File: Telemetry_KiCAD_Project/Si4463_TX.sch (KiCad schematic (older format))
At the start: 14 parts, among them U2 Si4463, Y1 30MHz

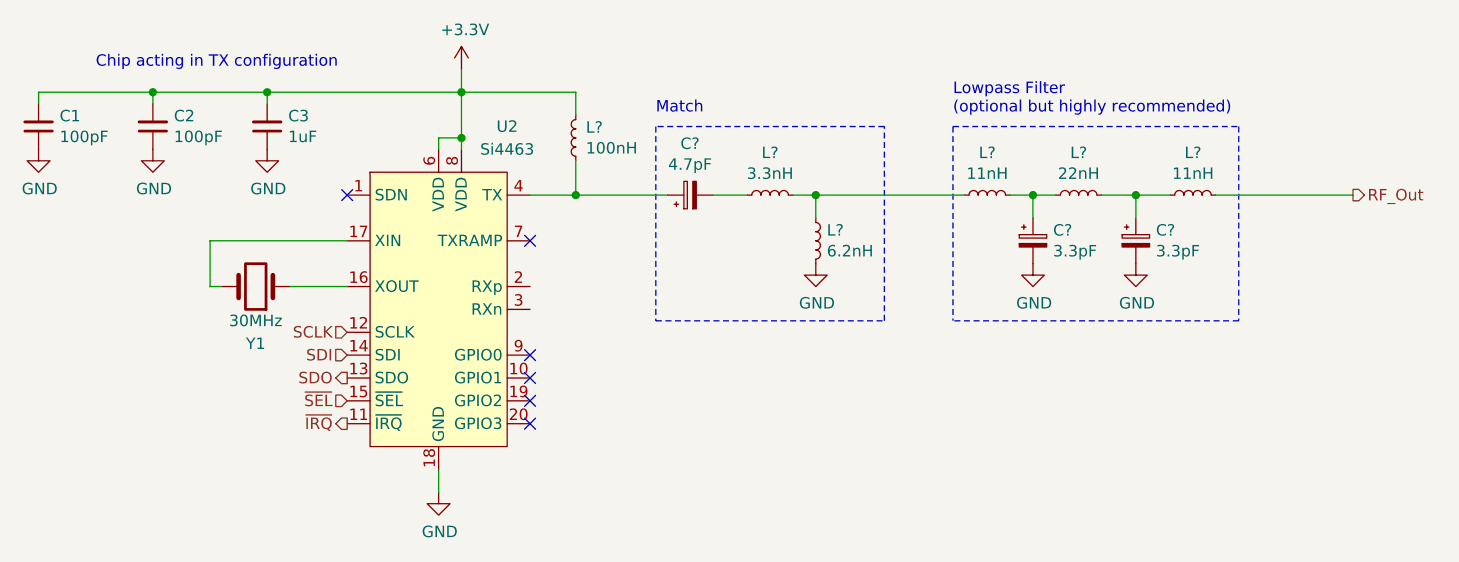
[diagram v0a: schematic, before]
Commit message: Added TX/RX matching network passives to PCB
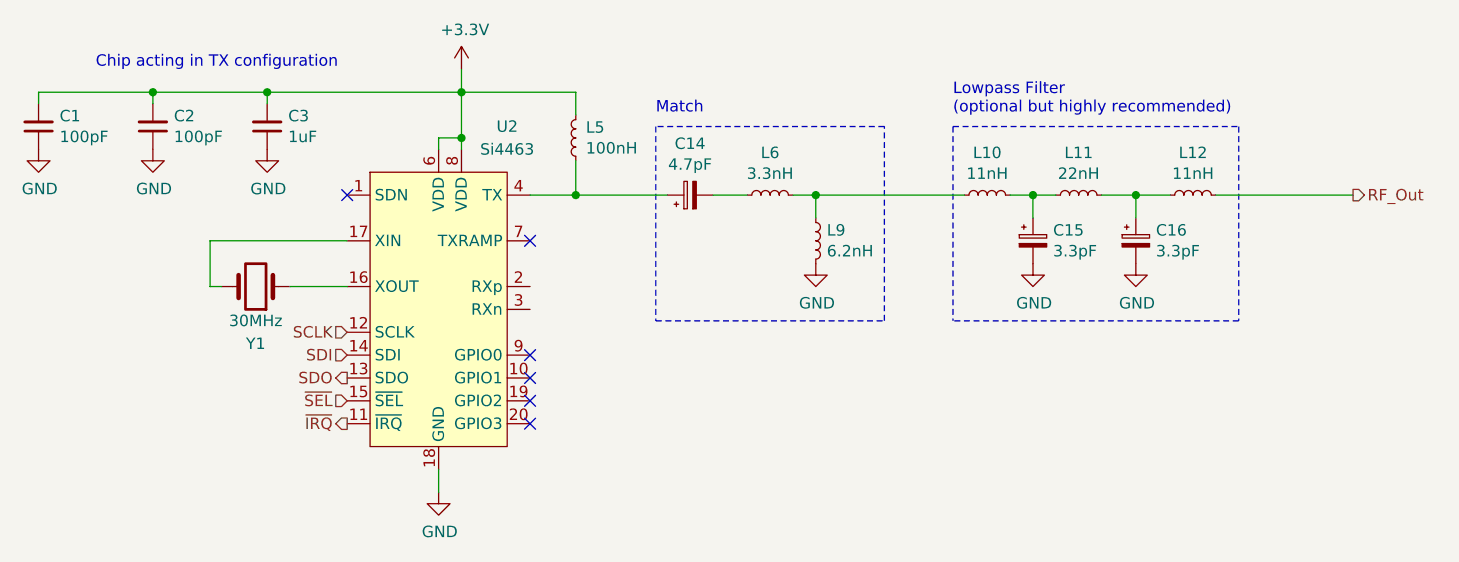
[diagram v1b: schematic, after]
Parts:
- C14, C15, C16: renamed from C?; footprint (none) -> Capacitor_SMD:C_0603_1608Metric
- L10, L11, L12, L5, L6, L9: renamed from L?; footprint (none) -> Inductor_SMD:L_0603_1608Metric
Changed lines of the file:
@@
 $Comp
 L power:GND #PWR0104
-U 1 1 619DAEC1
+U 1 1 61AFA3CA
 P 6150 4450
-AR Path="/619D9C89/619DAEC1" Ref="#PWR0104"  Part="1"
-AR Path="/61A0416A/619DAEC1" Ref="#PWR0116"  Part="1"
+AR Path="/619D9C89/61AFA3CA" Ref="#PWR0104"  Part="1"
+AR Path="/61A0416A/61AFA3CA" Ref="#PWR0116"  Part="1"
 F 0 "#PWR0104" H 6150 4200 50  0001 C CNN
 F 1 "GND" H 6155 4277 50  0000 C CNN
@@
 $Comp
 L Device:C_Small C3
-U 1 1 619F7D57
+U 1 1 61AFA3CC
 P 5400 2850
-AR Path="/619D9C89/619F7D57" Ref="C3"  Part="1"
-AR Path="/61A0416A/619F7D57" Ref="C13"  Part="1"
+AR Path="/619D9C89/61AFA3CC" Ref="C3"  Part="1"
+AR Path="/61A0416A/61AFA3CC" Ref="C13"  Part="1"
 F 0 "C3" H 5308 2804 50  0000 R CNN
 F 1 "1uF" H 5308 2895 50  0000 R CNN
@@
 $Comp
 L Device:C_Small C2
-U 1 1 619F860E
+U 1 1 61AFA3CD
 P 4900 2850
-AR Path="/619D9C89/619F860E" Ref="C2"  Part="1"
-AR Path="/61A0416A/619F860E" Ref="C12"  Part="1"
+AR Path="/619D9C89/61AFA3CD" Ref="C2"  Part="1"
+AR Path="/61A0416A/61AFA3CD" Ref="C12"  Part="1"
 F 0 "C2" H 4808 2804 50  0000 R CNN
 F 1 "100pF" H 4808 2895 50  0000 R CNN
@@
 $Comp
 L Device:C_Small C1
-U 1 1 619F8BD8
+U 1 1 61AFA3CE
 P 4400 2850
-AR Path="/619D9C89/619F8BD8" Ref="C1"  Part="1"
-AR Path="/61A0416A/619F8BD8" Ref="C11"  Part="1"
+AR Path="/619D9C89/61AFA3CE" Ref="C1"  Part="1"
+AR Path="/61A0416A/61AFA3CE" Ref="C11"  Part="1"
 F 0 "C1" H 4308 2804 50  0000 R CNN
 F 1 "100pF" H 4308 2895 50  0000 R CNN
@@
 $Comp
 L power:GND #PWR0109
-U 1 1 619F9745
+U 1 1 61AFA3CF
 P 4400 2950
-AR Path="/619D9C89/619F9745" Ref="#PWR0109"  Part="1"
-AR Path="/61A0416A/619F9745" Ref="#PWR0121"  Part="1"
+AR Path="/619D9C89/61AFA3CF" Ref="#PWR0109"  Part="1"
+AR Path="/61A0416A/61AFA3CF" Ref="#PWR0121"  Part="1"
 F 0 "#PWR0109" H 4400 2700 50  0001 C CNN
 F 1 "GND" H 4405 2777 50  0000 C CNN
@@
 $Comp
 L power:GND #PWR0111
-U 1 1 619F9CE2
+U 1 1 61AFA3D1
 P 5400 2950
-AR Path="/619D9C89/619F9CE2" Ref="#PWR0111"  Part="1"
-AR Path="/61A0416A/619F9CE2" Ref="#PWR0123"  Part="1"
+AR Path="/619D9C89/61AFA3D1" Ref="#PWR0111"  Part="1"
+AR Path="/61A0416A/61AFA3D1" Ref="#PWR0123"  Part="1"
 F 0 "#PWR0111" H 5400 2700 50  0001 C CNN
 F 1 "GND" H 5405 2777 50  0000 C CNN
@@
 NoConn ~ 5750 3150
 $Comp
-L Device:L_Small L?
+L Device:L_Small L5
 U 1 1 61AC1A40
 P 6750 2900
-AR Path="/619D9C89/61AC1A40" Ref="L?"  Part="1"
+AR Path="/619D9C89/61AC1A40" Ref="L5"  Part="1"
 AR Path="/61A0416A/61AC1A40" Ref="L?"  Part="1"
-F 0 "L?" H 6706 2854 50  0000 R CNN
+F 0 "L5" H 6706 2854 50  0000 R CNN
 F 1 "100nH" H 6706 2945 50  0000 R CNN
-F 2 "" H 6750 2900 50  0001 C CNN
+F 2 "Inductor_SMD:L_0603_1608Metric" H 6750 2900 50  0001 C CNN
 F 3 "~" H 6750 2900 50  0001 C CNN
 	1    6750 2900
@@
 Connection ~ 6750 3150
 $Comp
-L Device:L_Small L?
+L Device:L_Small L6
 U 1 1 61AC64F7
 P 7600 3150
-AR Path="/619D9C89/61AC64F7" Ref="L?"  Part="1"
+AR Path="/619D9C89/61AC64F7" Ref="L6"  Part="1"
 AR Path="/61A0416A/61AC64F7" Ref="L?"  Part="1"
-F 0 "L?" V 7785 3150 50  0000 C CNN
+F 0 "L6" V 7785 3150 50  0000 C CNN
 F 1 "3.3nH" V 7694 3150 50  0000 C CNN
-F 2 "" H 7600 3150 50  0001 C CNN
+F 2 "Inductor_SMD:L_0603_1608Metric" H 7600 3150 50  0001 C CNN
 F 3 "~" H 7600 3150 50  0001 C CNN
 	1    7600 3150
@@
 	7350 3150 7500 3150
 $Comp
-L Device:L_Small L?
+L Device:L_Small L9
 U 1 1 61AC7786
 P 7800 3350
-AR Path="/619D9C89/61AC7786" Ref="L?"  Part="1"
+AR Path="/619D9C89/61AC7786" Ref="L9"  Part="1"
 AR Path="/61A0416A/61AC7786" Ref="L?"  Part="1"
-F 0 "L?" H 7848 3396 50  0000 L CNN
+F 0 "L9" H 7848 3396 50  0000 L CNN
 F 1 "6.2nH" H 7848 3305 50  0000 L CNN
-F 2 "" H 7800 3350 50  0001 C CNN
+F 2 "Inductor_SMD:L_0603_1608Metric" H 7800 3350 50  0001 C CNN
 F 3 "~" H 7800 3350 50  0001 C CNN
 	1    7800 3350
@@
 	7800 3250 7800 3150
 $Comp
-L power:GND #PWR?
+L power:GND #PWR011
 U 1 1 61AC819F
 P 7800 3450
-AR Path="/619D9C89/61AC819F" Ref="#PWR?"  Part="1"
+AR Path="/619D9C89/61AC819F" Ref="#PWR011"  Part="1"
 AR Path="/61A0416A/61AC819F" Ref="#PWR?"  Part="1"
-F 0 "#PWR?" H 7800 3200 50  0001 C CNN
+F 0 "#PWR011" H 7800 3200 50  0001 C CNN
 F 1 "GND" H 7805 3277 50  0000 C CNN
 F 2 "" H 7800 3450 50  0001 C CNN
@@
 $EndComp
 $Comp
-L Device:L_Small L?
+L Device:L_Small L10
 U 1 1 61AC8B03
 P 8550 3150
-AR Path="/619D9C89/61AC8B03" Ref="L?"  Part="1"
+AR Path="/619D9C89/61AC8B03" Ref="L10"  Part="1"
 AR Path="/61A0416A/61AC8B03" Ref="L?"  Part="1"
-F 0 "L?" V 8735 3150 50  0000 C CNN
+F 0 "L10" V 8735 3150 50  0000 C CNN
 F 1 "11nH" V 8644 3150 50  0000 C CNN
-F 2 "" H 8550 3150 50  0001 C CNN
+F 2 "Inductor_SMD:L_0603_1608Metric" H 8550 3150 50  0001 C CNN
 F 3 "~" H 8550 3150 50  0001 C CNN
 	1    8550 3150
@@
 	8750 3250 8750 3150
 $Comp
-L power:GND #PWR?
+L power:GND #PWR012
 U 1 1 61ACB831
 P 8750 3450
-AR Path="/619D9C89/61ACB831" Ref="#PWR?"  Part="1"
+AR Path="/619D9C89/61ACB831" Ref="#PWR012"  Part="1"
 AR Path="/61A0416A/61ACB831" Ref="#PWR?"  Part="1"
-F 0 "#PWR?" H 8750 3200 50  0001 C CNN
+F 0 "#PWR012" H 8750 3200 50  0001 C CNN
 F 1 "GND" H 8755 3277 50  0000 C CNN
 F 2 "" H 8750 3450 50  0001 C CNN
@@
 $EndComp
 $Comp
-L Device:L_Small L?
+L Device:L_Small L11
 U 1 1 61ACBE23
 P 8950 3150
-AR Path="/619D9C89/61ACBE23" Ref="L?"  Part="1"
+AR Path="/619D9C89/61ACBE23" Ref="L11"  Part="1"
 AR Path="/61A0416A/61ACBE23" Ref="L?"  Part="1"
-F 0 "L?" V 9135 3150 50  0000 C CNN
+F 0 "L11" V 9135 3150 50  0000 C CNN
 F 1 "22nH" V 9044 3150 50  0000 C CNN
-F 2 "" H 8950 3150 50  0001 C CNN
+F 2 "Inductor_SMD:L_0603_1608Metric" H 8950 3150 50  0001 C CNN
 F 3 "~" H 8950 3150 50  0001 C CNN
 	1    8950 3150
@@
 	9200 3150 9200 3250
 $Comp
-L power:GND #PWR?
+L power:GND #PWR013
 U 1 1 61ACE820
 P 9200 3450
-AR Path="/619D9C89/61ACE820" Ref="#PWR?"  Part="1"
+AR Path="/619D9C89/61ACE820" Ref="#PWR013"  Part="1"
 AR Path="/61A0416A/61ACE820" Ref="#PWR?"  Part="1"
-F 0 "#PWR?" H 9200 3200 50  0001 C CNN
+F 0 "#PWR013" H 9200 3200 50  0001 C CNN
 F 1 "GND" H 9205 3277 50  0000 C CNN
 F 2 "" H 9200 3450 50  0001 C CNN
@@
 $EndComp
 $Comp
-L Device:L_Small L?
+L Device:L_Small L12
 U 1 1 61ACEC52
 P 9450 3150
-AR Path="/619D9C89/61ACEC52" Ref="L?"  Part="1"
+AR Path="/619D9C89/61ACEC52" Ref="L12"  Part="1"
 AR Path="/61A0416A/61ACEC52" Ref="L?"  Part="1"
-F 0 "L?" V 9635 3150 50  0000 C CNN
+F 0 "L12" V 9635 3150 50  0000 C CNN
 F 1 "11nH" V 9544 3150 50  0000 C CNN
-F 2 "" H 9450 3150 50  0001 C CNN
+F 2 "Inductor_SMD:L_0603_1608Metric" H 9450 3150 50  0001 C CNN
 F 3 "~" H 9450 3150 50  0001 C CNN
 	1    9450 3150
@@
 Chip acting in TX configuration
 $Comp
-L Device:CP_Small C?
+L Device:CP_Small C15
 U 1 1 61AE96AB
 P 8750 3350
-F 0 "C?" H 8838 3396 50  0000 L CNN
+F 0 "C15" H 8838 3396 50  0000 L CNN
 F 1 "3.3pF" H 8838 3305 50  0000 L CNN
-F 2 "" H 8750 3350 50  0001 C CNN
+F 2 "Capacitor_SMD:C_0603_1608Metric" H 8750 3350 50  0001 C CNN
 F 3 "~" H 8750 3350 50  0001 C CNN
 	1    8750 3350
@@
 $EndComp
 $Comp
-L Device:CP_Small C?
+L Device:CP_Small C16
 U 1 1 61AEA802
 P 9200 3350
-F 0 "C?" H 9288 3396 50  0000 L CNN
+F 0 "C16" H 9288 3396 50  0000 L CNN
 F 1 "3.3pF" H 9288 3305 50  0000 L CNN
-F 2 "" H 9200 3350 50  0001 C CNN
+F 2 "Capacitor_SMD:C_0603_1608Metric" H 9200 3350 50  0001 C CNN
 F 3 "~" H 9200 3350 50  0001 C CNN
 	1    9200 3350
@@
 $EndComp
 $Comp
-L Device:CP_Small C?
+L Device:CP_Small C14
 U 1 1 61AEACA0
 P 7250 3150
-F 0 "C?" V 7475 3150 50  0000 C CNN
+F 0 "C14" V 7475 3150 50  0000 C CNN
 F 1 "4.7pF" V 7384 3150 50  0000 C CNN
-F 2 "" H 7250 3150 50  0001 C CNN
+F 2 "Capacitor_SMD:C_0603_1608Metric" H 7250 3150 50  0001 C CNN
 F 3 "~" H 7250 3150 50  0001 C CNN
 	1    7250 3150
